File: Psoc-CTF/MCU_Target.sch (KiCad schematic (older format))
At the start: 96 parts, among them IC1 CY8C4248LQI-BL583, J10 Conn_01x20, J11 Conn_01x20, J4 Conn_01x04, J5 USB3076-XX-X_REVC, J6 Conn_01x10, J7 Conn_01x04, J8 Conn_01x20, J9 Conn_01x20, P1 Power, P2 Analog, P3 Digital, P4 Digital, SW3 FSM4JSMATR, SW4 FSM4JSMATR, SW5 FSM4JSMATR, U4 FM24C04B-GTR, U5 CY7C65211-24LTXI, Y1 24MHz, Y2 32.768Khz

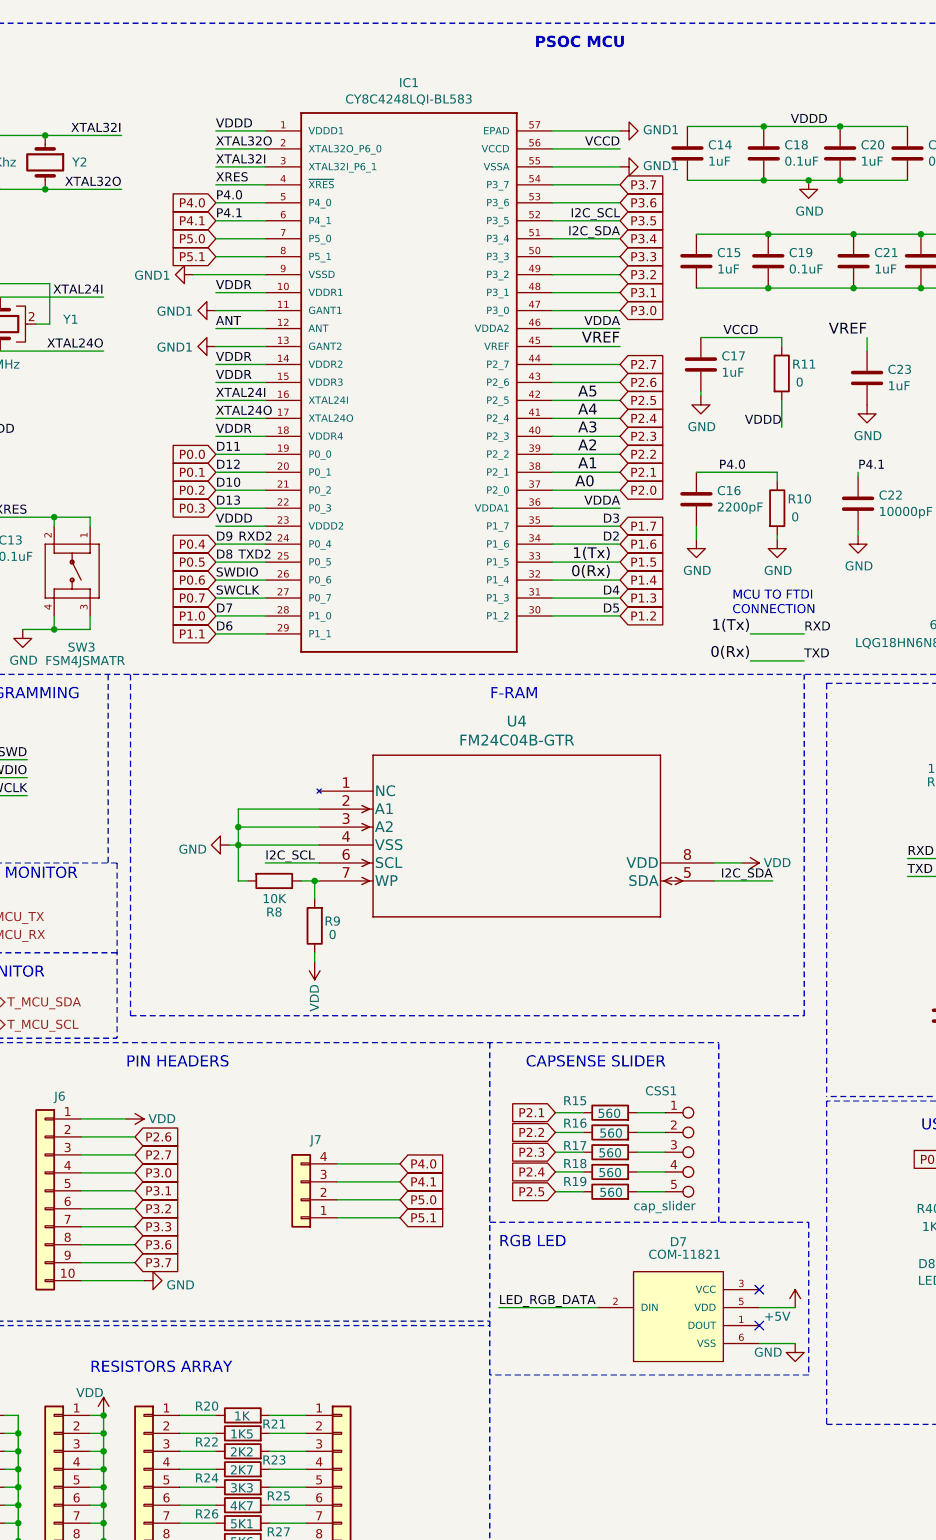
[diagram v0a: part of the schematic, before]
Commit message: Correcciones del retorno de tiera y medicion de corriente
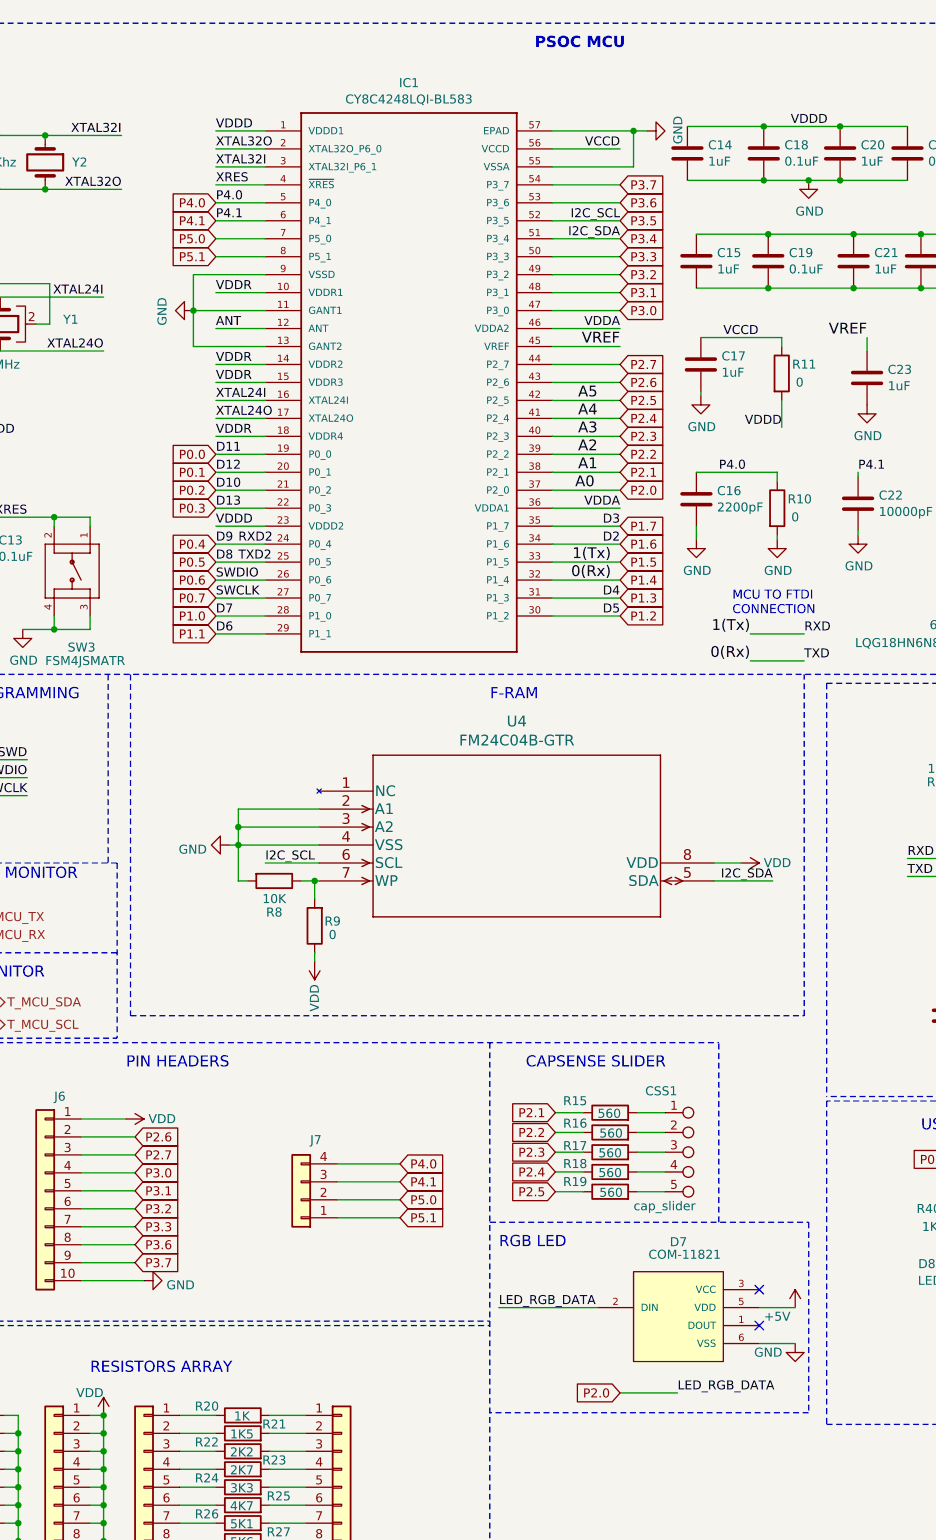
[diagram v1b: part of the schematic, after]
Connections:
- net GND1 is gone; now on net GND: IC1.11 (GANT1), IC1.13 (GANT2), IC1.55 (VSSA), IC1.57 (EPAD), IC1.9 (VSSD)
- net LED_RGB_DATA is gone; now on net P2.0: D7.2 (DIN)
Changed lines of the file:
@@
 	2575 2025 2300 2025
 Wire Wire Line
-	2575 2125 2300 2125
-Wire Wire Line
 	2575 2225 2300 2225
-Wire Wire Line
-	2575 2325 2300 2325
 Wire Wire Line
 	2575 2425 2300 2425
@@
 Wire Wire Line
 	4175 1225 4550 1225
-Wire Wire Line
-	4175 1325 4550 1325
-Wire Wire Line
-	4175 1125 4550 1125
 Wire Wire Line
 	4175 1425 4550 1425
@@
 	550  6200 5100 6200
 Wire Notes Line
-	5600 8050 3825 8050
-Wire Notes Line
-	5600 7200 5600 8050
+	5600 8260 3825 8260
 Text Notes 1800 6350 0    62   ~ 0
 PIN HEADERS
@@
 NoConn ~ 7950 5875
 NoConn ~ 7950 5975
-$Comp
-L power:GND1 #PWR058
-U 1 1 622855DE
-P 2300 2325
-F 0 "#PWR058" H 2300 2075 50  0001 C CNN
-F 1 "GND1" V 2305 2197 50  0000 R CNN
-F 2 "" H 2300 2325 50  0001 C CNN
-F 3 "" H 2300 2325 50  0001 C CNN
-	1    2300 2325
-	0    1    1    0
-$EndComp
-$Comp
-L power:GND1 #PWR057
-U 1 1 62285D2A
-P 2300 2125
-F 0 "#PWR057" H 2300 1875 50  0001 C CNN
-F 1 "GND1" V 2305 1997 50  0000 R CNN
-F 2 "" H 2300 2125 50  0001 C CNN
-F 3 "" H 2300 2125 50  0001 C CNN
-	1    2300 2125
-	0    1    1    0
-$EndComp
-$Comp
-L power:GND1 #PWR061
-U 1 1 622860AC
-P 4550 1125
-F 0 "#PWR061" H 4550 875 50  0001 C CNN
-F 1 "GND1" V 4555 997 50  0000 R CNN
-F 2 "" H 4550 1125 50  0001 C CNN
-F 3 "" H 4550 1125 50  0001 C CNN
-	1    4550 1125
-	0    -1   -1   0
-$EndComp
-$Comp
-L power:GND1 #PWR062
-U 1 1 622CDC9D
-P 4550 1325
-F 0 "#PWR062" H 4550 1075 50  0001 C CNN
-F 1 "GND1" V 4555 1197 50  0000 R CNN
-F 2 "" H 4550 1325 50  0001 C CNN
-F 3 "" H 4550 1325 50  0001 C CNN
-	1    4550 1325
-	0    -1   -1   0
-$EndComp
 Wire Wire Line
 	5275 3925 5575 3925
@@
 Text Label 2425 3525 0    50   ~ 0
 TXD2
-$Comp
-L power:GND1 #PWR0103
-U 1 1 623C2929
-P 2175 1925
-F 0 "#PWR0103" H 2175 1675 50  0001 C CNN
-F 1 "GND1" V 2180 1797 50  0000 R CNN
-F 2 "" H 2175 1925 50  0001 C CNN
-F 3 "" H 2175 1925 50  0001 C CNN
-	1    2175 1925
-	0    1    1    0
-$EndComp
 Text Label 8900 2925 0    60   ~ 0
 A4
@@
 Connection ~ 1675 8275
 Connection ~ 1200 10175
+Text Label 4870 8150 0    50   ~ 0
+LED_RGB_DATA
+Text GLabel 4550 8150 0    50   Input ~ 0
+P2.0
+Wire Notes Line
+	5600 7200 5600 8260
+Wire Wire Line
+	4550 8150 4870 8150
+$Comp
+L power:GND #PWR?
+U 1 1 625A71D9
+P 4700 1125
+AR Path="/625A71D9" Ref="#PWR?"  Part="1"
+AR Path="/62149449/625A71D9" Ref="#PWR?"  Part="1"
+F 0 "#PWR?" H 4700 875 50  0001 C CNN
+F 1 "GND" H 4705 952 50  0000 C CNN
+F 2 "" H 4700 1125 50  0001 C CNN
+F 3 "" H 4700 1125 50  0001 C CNN
+	1    4700 1125
+	0    -1   -1   0
+$EndComp
+Wire Wire Line
+	4175 1125 4625 1125
+Wire Wire Line
+	4625 1325 4625 1125
+Wire Wire Line
+	4175 1325 4625 1325
+Connection ~ 4625 1125
+Wire Wire Line
+	4625 1125 4700 1125
+$Comp
+L power:GND #PWR?
+U 1 1 6262817F
+P 2175 2125
+AR Path="/6262817F" Ref="#PWR?"  Part="1"
+AR Path="/62149449/6262817F" Ref="#PWR?"  Part="1"
+F 0 "#PWR?" H 2175 1875 50  0001 C CNN
+F 1 "GND" H 2180 1952 50  0000 C CNN
+F 2 "" H 2175 2125 50  0001 C CNN
+F 3 "" H 2175 2125 50  0001 C CNN
+	1    2175 2125
+	0    1    1    0
+$EndComp
+Wire Wire Line
+	2175 2125 2175 1925
+Wire Wire Line
+	2175 2125 2575 2125
+Wire Wire Line
+	2175 2125 2175 2325
+Wire Wire Line
+	2175 2325 2575 2325
+Connection ~ 2175 2125
 $EndSCHEMATC
